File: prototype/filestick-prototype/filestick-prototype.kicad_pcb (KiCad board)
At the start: 4 copper layers, 85 x 75 mm, 54 parts, among them J1 DIN-5, J2 DIN-5, J3 GPIO header 1, J4 UART header, J5 GPIO header 2, J6 SPI header, Q1 2N7002, Q2 2N7002, Q3 2N7002, Q4 2N7002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

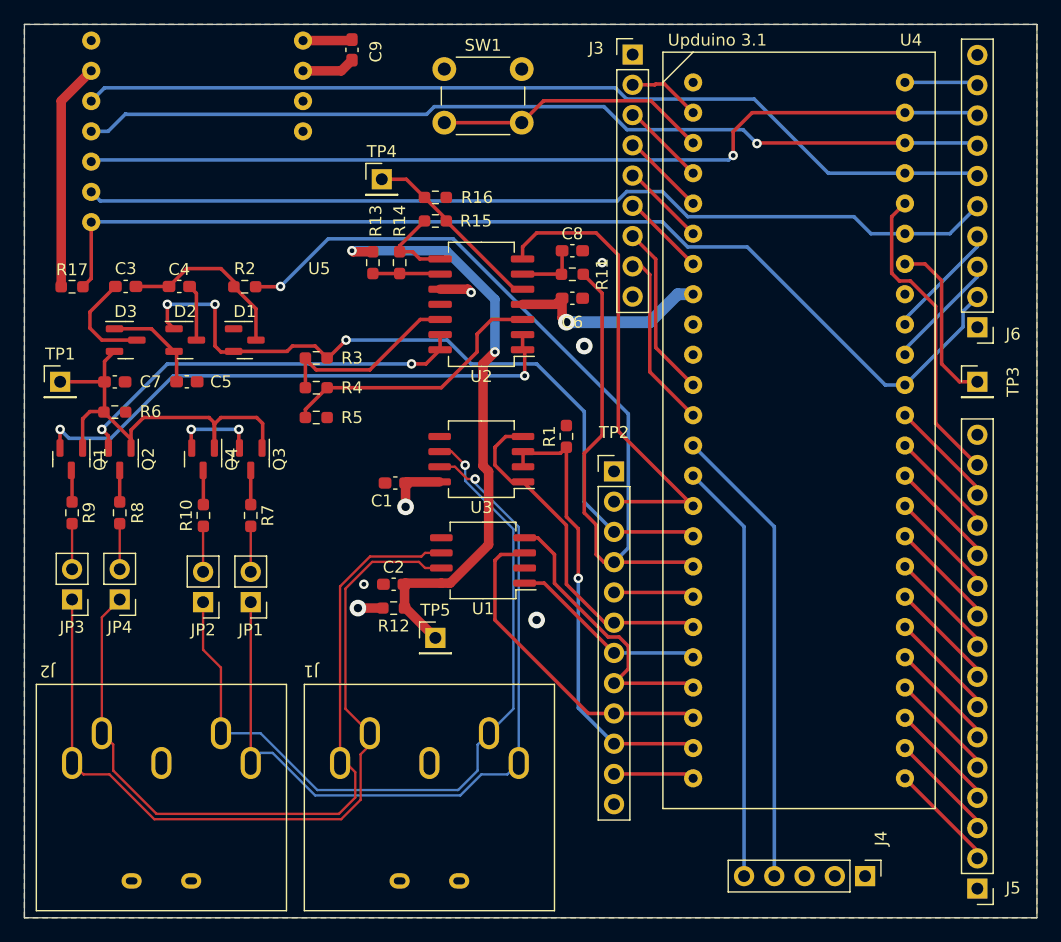
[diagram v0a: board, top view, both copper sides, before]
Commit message: clamp collision detection at 3v3, add leds etc
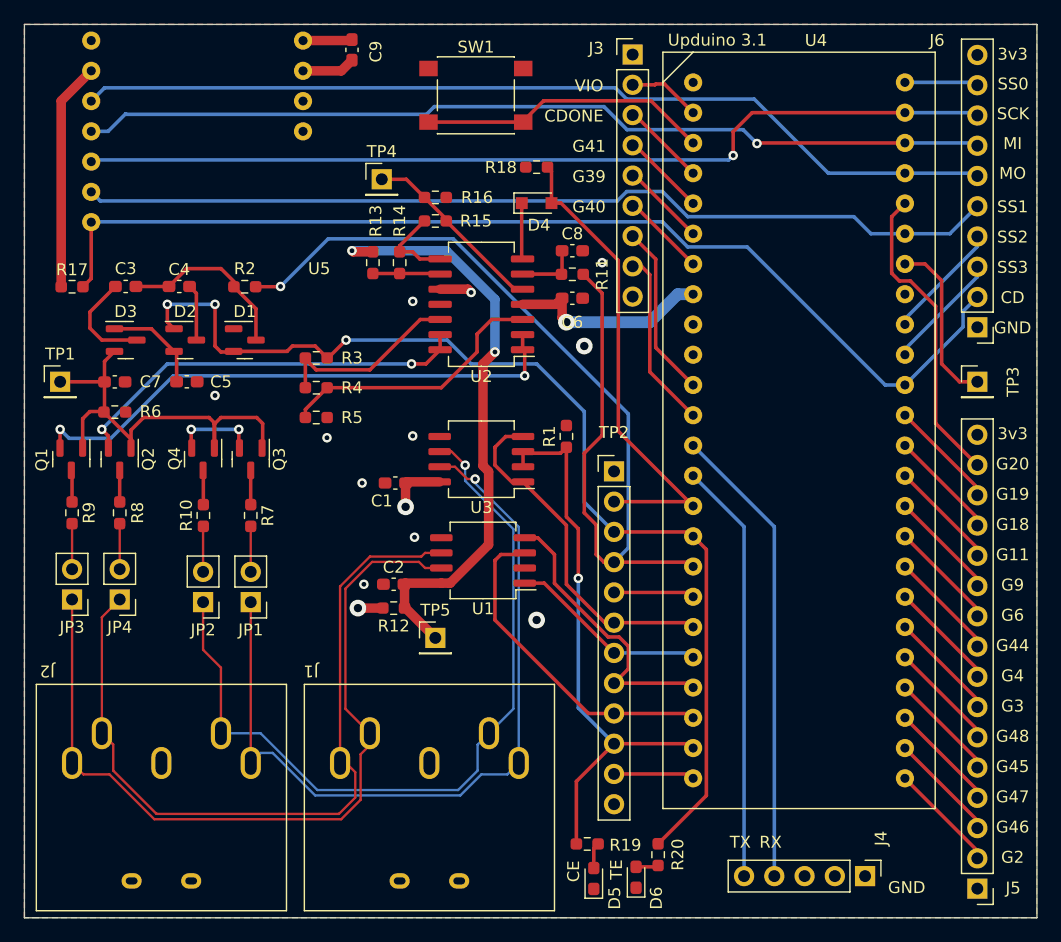
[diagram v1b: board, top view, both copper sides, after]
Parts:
- added D4: D_Zener 3.3v, Diode_SMD:D_SOD-323_HandSoldering, F.Cu at (148.0, 67.0)
- added D5: LED, LED_SMD:LED_0603_1608Metric_Pad1.05x0.95mm_HandSolder, F.Cu at (152.8, 123.7)
- added D6: LED, LED_SMD:LED_0603_1608Metric_Pad1.05x0.95mm_HandSolder, F.Cu at (156.3, 123.6)
- added R18: 1k, Resistor_SMD:R_0603_1608Metric_Pad0.98x0.95mm_HandSolder, F.Cu at (148.0, 64.0)
- added R19: 560, Resistor_SMD:R_0603_1608Metric_Pad0.98x0.95mm_HandSolder, F.Cu at (152.2, 120.8)
- added R20: 560, Resistor_SMD:R_0603_1608Metric_Pad0.98x0.95mm_HandSolder, F.Cu at (158.2, 121.7)
- SW1: footprint Button_Switch_THT:SW_PUSH_6mm -> Button_Switch_SMD:SW_Push_1P1T_NO_6x6mm_H9.5mm
- moved SW1 3.44 mm to (142.9, 58.0)
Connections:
- J1 pad G1: GND -> (no net)
- J1 pad G2: GND -> (no net)
- J2 pad G1: GND -> (no net)
- J2 pad G2: GND -> (no net)
- U2 pad 7: /COLLISION_DETECT -> /COLLISION_DETECT_5V
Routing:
- net /TERM_EN: track 62.6 -> 90.6 mm
- net /ECONET_CLKEN: track 38.5 -> 48.2 mm
- net /COLLISION_DETECT_5V: track 0.00 -> 4.72 mm
- net Net-(D5-Pad2): track 0.00 -> 2.18 mm
- net Net-(D6-Pad2): track 0.00 -> 1.90 mm
- net Net-(SW1-Pad2): track 23.1 -> 24.6 mm
- net GND: vias 4 -> 10
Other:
- board text added: "3v3"
- board text added: "CD"
- board text added: "CDONE"
- board text added: "CE"
- board text added: "G11"
- board text added: "G18"
- board text added: "G19"
- board text added: "G2"
- board text added: "G20"
- board text added: "G3"
- board text added: "G39"
- board text added: "G4"
- board text added: "G40"
- board text added: "G41"
- board text added: "G44"
- board text added: "G45"
- board text added: "G46"
- board text added: "G47"
- board text added: "G48"
- board text added: "G6"
- board text added: "G9"
- board text added: "GND"
- board text added: "MI"
- board text added: "MO"
- board text added: "RX"
- board text added: "SCK"
- board text added: "SS0"
- board text added: "SS1"
- board text added: "SS2"
- board text added: "SS3"
- board text added: "TE"
- board text added: "TX"
- board text added: "VIO"

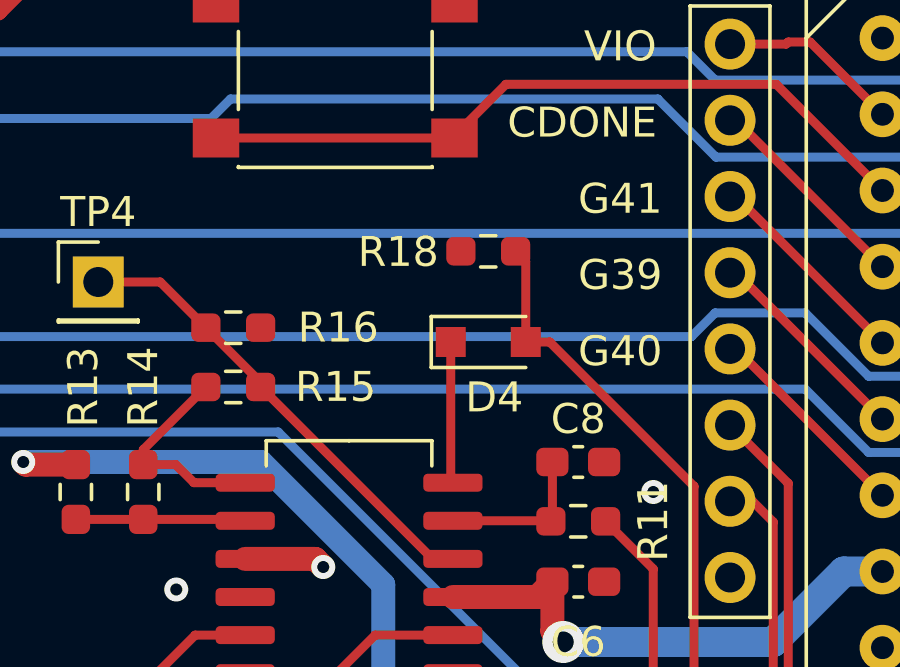
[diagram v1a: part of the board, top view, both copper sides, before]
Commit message: better level shifter
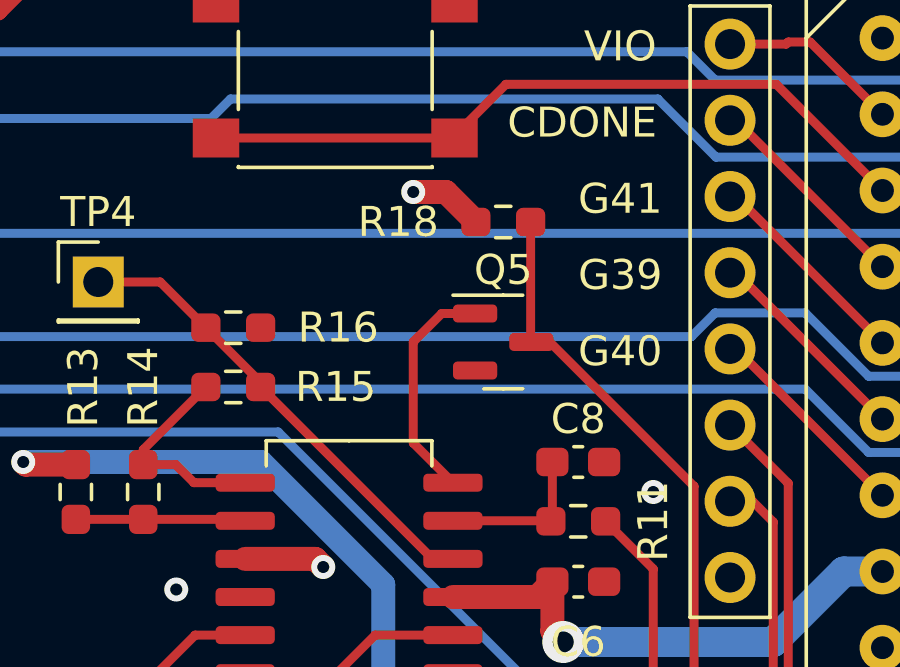
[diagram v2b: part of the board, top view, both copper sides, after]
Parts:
- removed D4: D_Zener 3.3v, Diode_SMD:D_SOD-323_HandSoldering
- added Q5: 2N7002, Package_TO_SOT_SMD:SOT-23, F.Cu at (148.5, 67.0)
- moved R18 1.10 mm to (148.5, 63.0), turned to 0 degrees
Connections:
- R18 pad 1: /COLLISION_DETECT -> +3.3V
- R18 pad 2: GND -> /COLLISION_DETECT
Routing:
- net /COLLISION_DETECT_5V: track 4.72 -> 7.69 mm
- net +3.3V: track 33.4 -> 35.9 mm, vias 3 -> 4
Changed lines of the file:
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@@
-    )
-  )
-  (footprint "Diode_SMD:D_SOD-323_HandSoldering" (layer "F.Cu")
-    (at 148 67)
-    (descr "SOD-323")
-    (tags "SOD-323")
-    (property "Sheetfile" "filestick-prototype.kicad_sch")
-    (property "Sheetname" "")
-    (attr smd)
-    (fp_text reference "D4" (at 0.2 1.85) (layer "F.SilkS")
-      (effects (font (size 1 1) (thickness 0.15)))
-    )
-    (fp_text value "D_Zener 3.3v" (at 0.1 1.9) (layer "F.Fab")
-      (effects (font (size 1 1) (thickness 0.15)))
-    )
-    (fp_text user "${REFERENCE}" (at 0 -1.85) (layer "F.Fab")
-      (effects (font (size 1 1) (thickness 0.15)))
-    )
-    (fp_line (start -1.9 -0.85) (end -1.9 0.85) (layer "F.SilkS") (width 0.12))
-    (fp_line (start -1.9 -0.85) (end 1.25 -0.85) (layer "F.SilkS") (width 0.12))
-    (fp_line (start -1.9 0.85) (end 1.25 0.85) (layer "F.SilkS") (width 0.12))
-    (fp_line (start -2 -0.95) (end -2 0.95) (layer "F.CrtYd") (width 0.05))
-    (fp_line (start -2 -0.95) (end 2 -0.95) (layer "F.CrtYd") (width 0.05))
-    (fp_line (start 2 -0.95) (end 2 0.95) (layer "F.CrtYd") (width 0.05))
-    (fp_line (start -2 0.95) (end 2 0.95) (layer "F.CrtYd") (width 0.05))
-    (fp_line (start 0.2 -0.35) (end 0.2 0.35) (layer "F.Fab") (width 0.1))
-    (fp_line (start -0.3 0) (end 0.2 -0.35) (layer "F.Fab") (width 0.1))
-    (fp_line (start -0.3 -0.35) (end -0.3 0.35) (layer "F.Fab") (width 0.1))
-    (fp_line (start -0.9 0.7) (end -0.9 -0.7) (layer "F.Fab") (width 0.1))
-    (fp_line (start 0.9 -0.7) (end 0.9 0.7) (layer "F.Fab") (width 0.1))
-    (fp_line (start -0.3 0) (end -0.5 0) (layer "F.Fab") (width 0.1))
-    (fp_line (start -0.9 -0.7) (end 0.9 -0.7) (layer "F.Fab") (width 0.1))
-    (fp_line (start 0.2 0) (end 0.45 0) (layer "F.Fab") (width 0.1))
-    (fp_line (start 0.2 0.35) (end -0.3 0) (layer "F.Fab") (width 0.1))
-    (fp_line (start 0.9 0.7) (end -0.9 0.7) (layer "F.Fab") (width 0.1))
-    (pad "1" smd rect (at -1.25 0) (size 1 1) (layers "F.Cu" "F.Paste" "F.Mask")
-      (net 79 "/COLLISION_DETECT_5V") (pinfunction "K") (pintype "passive"))
-    (pad "2" smd rect (at 1.25 0) (size 1 1) (layers "F.Cu" "F.Paste" "F.Mask")
-      (net 69 "/COLLISION_DETECT") (pinfunction "A") (pintype "passive"))
-    (model "${KICAD6_3DMODEL_DIR}/Diode_SMD.3dshapes/D_SOD-323.wrl"
-      (offset (xyz 0 0 0))
-      (scale (xyz 1 1 1))
-      (rotate (xyz 0 0 0))
     )
   )
@@
   )
   (footprint "Package_TO_SOT_SMD:SOT-23" (layer "F.Cu")
+    (at 148.5 67)
+    (descr "SOT, 3 Pin (https://www.jedec.org/system/files/docs/to-236h.pdf variant AB), generated with kicad-footprint-generator ipc_gullwing_generator.py")
+    (tags "SOT TO_SOT_SMD")
+    (property "Sheetfile" "filestick-prototype.kicad_sch")
+    (property "Sheetname" "")
+    (attr smd)
+    (fp_text reference "Q5" (at 0 -2.4) (layer "F.SilkS")
+      (effects (font (size 1 1) (thickness 0.15)))
+    )
+    (fp_text value "2N7002" (at 0 2.4) (layer "F.Fab")
+      (effects (font (size 1 1) (thickness 0.15)))
+    )
+    (fp_text user "${REFERENCE}" (at 0 0) (layer "F.Fab")
+      (effects (font (size 0.32 0.32) (thickness 0.05)))
+    )
+    (fp_line (start 0 -1.56) (end -1.675 -1.56) (layer "F.SilkS") (width 0.12))
+    (fp_line (start 0 1.56) (end -0.65 1.56) (layer "F.SilkS") (width 0.12))
+    (fp_line (start 0 1.56) (end 0.65 1.56) (layer "F.SilkS") (width 0.12))
+    (fp_line (start 0 -1.56) (end 0.65 -1.56) (layer "F.SilkS") (width 0.12))
+    (fp_line (start 1.92 1.7) (end 1.92 -1.7) (layer "F.CrtYd") (width 0.05))
+    (fp_line (start -1.92 -1.7) (end -1.92 1.7) (layer "F.CrtYd") (width 0.05))
+    (fp_line (start 1.92 -1.7) (end -1.92 -1.7) (layer "F.CrtYd") (width 0.05))
+    (fp_line (start -1.92 1.7) (end 1.92 1.7) (layer "F.CrtYd") (width 0.05))
+    (fp_line (start -0.65 -1.125) (end -0.325 -1.45) (layer "F.Fab") (width 0.1))
+    (fp_line (start -0.325 -1.45) (end 0.65 -1.45) (layer "F.Fab") (width 0.1))
+    (fp_line (start -0.65 1.45) (end -0.65 -1.125) (layer "F.Fab") (width 0.1))
+    (fp_line (start 0.65 -1.45) (end 0.65 1.45) (layer "F.Fab") (width 0.1))
+    (fp_line (start 0.65 1.45) (end -0.65 1.45) (layer "F.Fab") (width 0.1))
+    (pad "1" smd roundrect (at -0.9375 -0.95) (size 1.475 0.6) (layers "F.Cu" "F.Paste" "F.Mask") (roundrect_rratio 0.25)
+      (net 79 "/COLLISION_DETECT_5V") (pinfunction "G") (pintype "input"))
+    (pad "2" smd roundrect (at -0.9375 0.95) (size 1.475 0.6) (layers "F.Cu" "F.Paste" "F.Mask") (roundrect_rratio 0.25)
+      (net 2 "GND") (pinfunction "S") (pintype "passive"))
+    (pad "3" smd roundrect (at 0.9375 0) (size 1.475 0.6) (layers "F.Cu" "F.Paste" "F.Mask") (roundrect_rratio 0.25)
+      (net 69 "/COLLISION_DETECT") (pinfunction "D") (pintype "passive"))
+    (model "${KICAD6_3DMODEL_DIR}/Package_TO_SOT_SMD.3dshapes/SOT-23.wrl"
+      (offset (xyz 0 0 0))
+      (scale (xyz 1 1 1))
+      (rotate (xyz 0 0 0))
+    )
+  )
+  (footprint "Package_TO_SOT_SMD:SOT-23" (layer "F.Cu")
     (at 113 88.5 -90)
     (descr "SOT, 3 Pin (https://www.jedec.org/system/files/docs/to-236h.pdf variant AB), generated with kicad-footprint-generator ipc_gullwing_generator.py")
@@
   )
   (footprint "Resistor_SMD:R_0603_1608Metric_Pad0.98x0.95mm_HandSolder" (layer "F.Cu")
-    (at 148 63.9775 180)
+    (at 148.5 63)
     (descr "Resistor SMD 0603 (1608 Metric), square (rectangular) end terminal, IPC_7351 nominal with elongated pad for handsoldering. (Body size source: IPC-SM-782 page 72, https://www.pcb-3d.com/wordpress/wp-content/uploads/ipc-sm-782a_amendment_1_and_2.pdf), generated with kicad-footprint-generator")
     (tags "resistor handsolder")
@@
     (property "Sheetname" "")
     (attr smd)
-    (fp_text reference "R18" (at 3 -0.0225) (layer "F.SilkS")
+    (fp_text reference "R18" (at -3.5 0) (layer "F.SilkS")
       (effects (font (size 1 1) (thickness 0.15)))
     )
@@
     (fp_line (start -0.8 0.4125) (end -0.8 -0.4125) (layer "F.Fab") (width 0.1))
     (fp_line (start -0.8 -0.4125) (end 0.8 -0.4125) (layer "F.Fab") (width 0.1))
-    (pad "1" smd roundrect (at -0.9125 0 180) (size 0.975 0.95) (layers "F.Cu" "F.Paste" "F.Mask") (roundrect_rratio 0.25)
+    (pad "1" smd roundrect (at -0.9125 0) (size 0.975 0.95) (layers "F.Cu" "F.Paste" "F.Mask") (roundrect_rratio 0.25)
+      (net 1 "+3.3V") (pintype "passive"))
+    (pad "2" smd roundrect (at 0.9125 0) (size 0.975 0.95) (layers "F.Cu" "F.Paste" "F.Mask") (roundrect_rratio 0.25)
       (net 69 "/COLLISION_DETECT") (pintype "passive"))
-    (pad "2" smd roundrect (at 0.9125 0 180) (size 0.975 0.95) (layers "F.Cu" "F.Paste" "F.Mask") (roundrect_rratio 0.25)
-      (net 2 "GND") (pintype "passive"))
     (model "${KICAD6_3DMODEL_DIR}/Resistor_SMD.3dshapes/R_0603_1608Metric.wrl"
       (offset (xyz 0 0 0))
@@
   (segment (start 139.8975 74.23) (end 142.23 74.23) (width 0.8) (layer "F.Cu") (net 1))
   (segment (start 139.86 90.405) (end 137.095 90.405) (width 0.8) (layer "F.Cu") (net 1))
+  (segment (start 146.5875 62) (end 147.5875 63) (width 0.8) (layer "F.Cu") (net 1))
   (segment (start 131.6025 55.8975) (end 132.5 55) (width 0.8) (layer "F.Cu") (net 1))
   (segment (start 133 101) (end 135.0875 101) (width 0.8) (layer "F.Cu") (net 1))
@@
   (segment (start 108.0875 58.42) (end 110.61 55.8975) (width 0.8) (layer "F.Cu") (net 1))
   (segment (start 108.0875 74.0225) (end 108.0875 58.42) (width 0.8) (layer "F.Cu") (net 1))
+  (segment (start 145.5 62) (end 146.5875 62) (width 0.8) (layer "F.Cu") (net 1))
+  (via (at 145.5 62) (size 0.8) (drill 0.4) (layers "F.Cu" "B.Cu") (free) (net 1))
   (via (at 142.5 74.5) (size 0.8) (drill 0.4) (layers "F.Cu" "B.Cu") (net 1))
   (via (at 133 101) (size 1.4) (drill 0.7) (layers "F.Cu" "B.Cu") (free) (net 1))
@@
   (segment (start 154.86 71.81) (end 154.86 86.15) (width 0.3) (layer "F.Cu") (net 69))
   (segment (start 160.775 92.065) (end 161.14 92.43) (width 0.3) (layer "F.Cu") (net 69))
+  (segment (start 149.4125 66.975) (end 149.4375 67) (width 0.3) (layer "F.Cu") (net 69))
   (segment (start 150.05 67) (end 154.86 71.81) (width 0.3) (layer "F.Cu") (net 69))
+  (segment (start 149.4125 63) (end 149.4125 66.975) (width 0.3) (layer "F.Cu") (net 69))
   (segment (start 154.5 92.065) (end 160.775 92.065) (width 0.3) (layer "F.Cu") (net 69))
   (segment (start 154.86 86.15) (end 161.14 92.43) (width 0.3) (layer "F.Cu") (net 69))
-  (segment (start 148.9125 63.9775) (end 149.25 64.315) (width 0.3) (layer "F.Cu") (net 69))
-  (segment (start 149.25 67) (end 150.05 67) (width 0.3) (layer "F.Cu") (net 69))
-  (segment (start 149.25 64.315) (end 149.25 67) (width 0.3) (layer "F.Cu") (net 69))
   (segment (start 160.775 99.685) (end 161.14 100.05) (width 0.3) (layer "F.Cu") (net 70))
   (segment (start 154.5 99.685) (end 160.775 99.685) (width 0.3) (layer "F.Cu") (net 70))
@@
   (segment (start 180.61 72.11) (end 182 73.5) (width 0.3) (layer "F.Cu") (net 76))
   (segment (start 183.5 82) (end 185 82) (width 0.3) (layer "F.Cu") (net 76))
-  (segment (start 146.75 71.6175) (end 146.75 67) (width 0.3) (layer "F.Cu") (net 79))
-  (segment (start 146.8225 71.69) (end 146.75 71.6175) (width 0.3) (layer "F.Cu") (net 79))
+  (segment (start 147.5625 66.05) (end 146.45 66.05) (width 0.3) (layer "F.Cu") (net 79))
+  (segment (start 145.5 70.3675) (end 146.8225 71.69) (width 0.3) (layer "F.Cu") (net 79))
+  (segment (start 146.45 66.05) (end 145.5 67) (width 0.3) (layer "F.Cu") (net 79))
+  (segment (start 145.5 67) (end 145.5 70.3675) (width 0.3) (layer "F.Cu") (net 79))
   (segment (start 152.8 121.1625) (end 153.1625 120.8) (width 0.3) (layer "F.Cu") (net 80))
   (segment (start 152.8 122.825) (end 152.8 121.1625) (width 0.3) (layer "F.Cu") (net 80))
